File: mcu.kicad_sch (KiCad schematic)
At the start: 30 parts, among them J301 CONN_MCU_SERIAL, J302 CONN_EXT, SW301 SW_RST, SW302 SW_BOOT0, U301 STM32F765IITx, Y301 25MHz

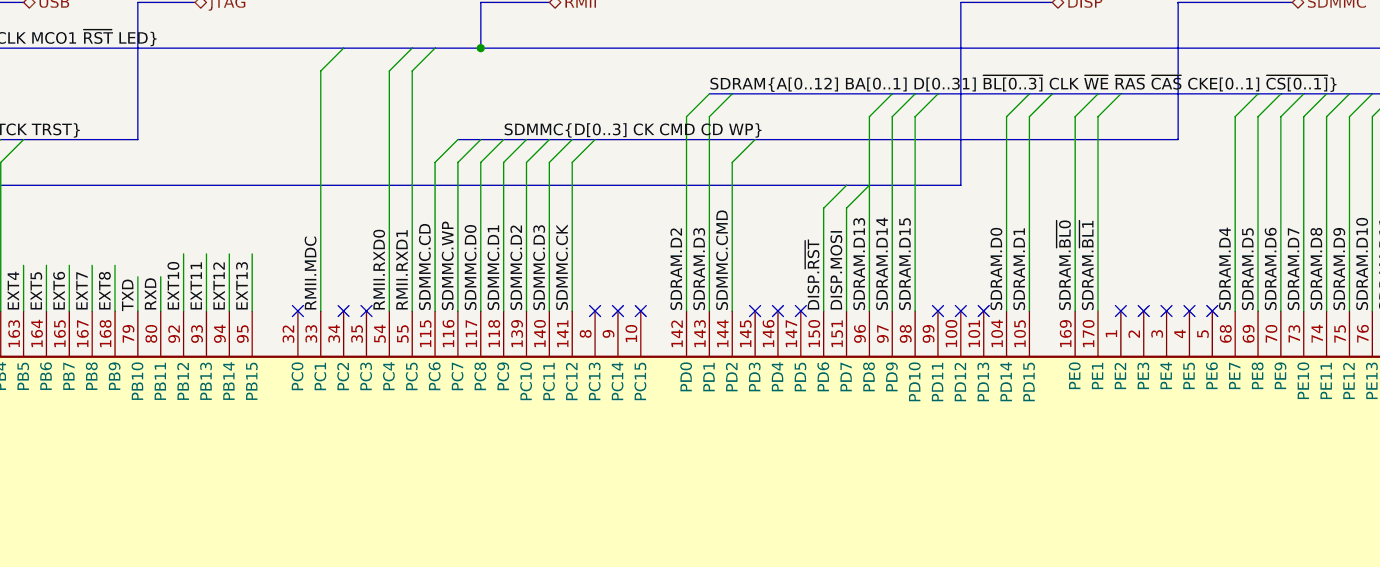
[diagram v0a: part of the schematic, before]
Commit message: Fix missing EXT9 connection, move EXT9-13 to PEx, route EXT connector.
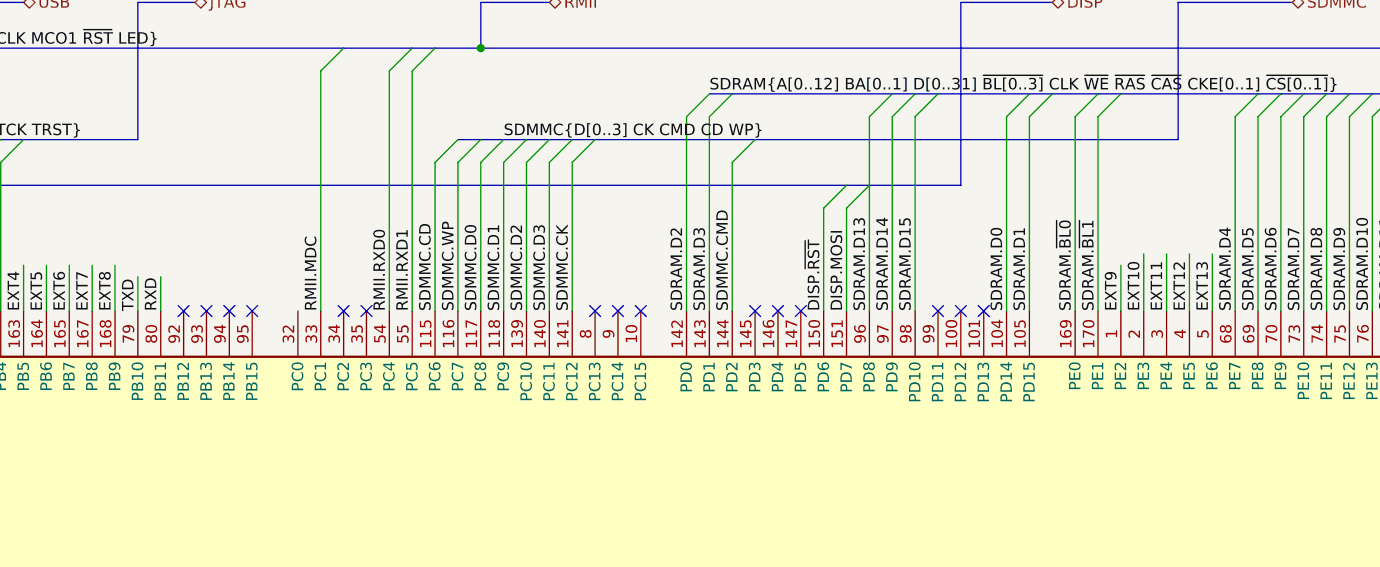
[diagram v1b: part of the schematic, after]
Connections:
- net EXT10: now also U301.2 (PE3); no longer U301.92 (PB12)
- net EXT11: now also U301.3 (PE4); no longer U301.93 (PB13)
- net EXT12: now also U301.4 (PE5); no longer U301.94 (PB14)
- net EXT13: now also U301.5 (PE6); no longer U301.95 (PB15)
- net EXT9: now also U301.1 (PE2)
- no-connect marks 26 -> 24
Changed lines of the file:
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@@
   (no_connect (at 176.53 50.8))
   (no_connect (at 207.01 124.46))
+  (no_connect (at 133.35 50.8))
   (no_connect (at 212.09 50.8))
   (no_connect (at 143.51 50.8))
@@
   (no_connect (at 250.19 124.46))
   (no_connect (at 212.09 124.46))
-  (no_connect (at 232.41 50.8))
   (no_connect (at 171.45 50.8))
-  (no_connect (at 237.49 50.8))
-  (no_connect (at 240.03 50.8))
   (no_connect (at 196.85 124.46))
-  (no_connect (at 229.87 50.8))
+  (no_connect (at 128.27 50.8))
   (no_connect (at 120.65 170.18))
-  (no_connect (at 234.95 50.8))
+  (no_connect (at 125.73 50.8))
   (no_connect (at 194.31 50.8))
   (no_connect (at 189.23 124.46))
@@
   (no_connect (at 191.77 50.8))
   (no_connect (at 204.47 124.46))
-  (no_connect (at 138.43 50.8))
+  (no_connect (at 130.81 50.8))
   (bus_entry (at 82.55 26.67) (size -2.54 2.54)
     (stroke (width 0) (type default) (color 0 0 0 0))
@@
     (stroke (width 0) (type default) (color 0 0 0 0))
   )
+  (wire (pts (xy 234.95 44.45) (xy 234.95 50.8))
+    (stroke (width 0) (type default) (color 0 0 0 0))
+  )
   (wire (pts (xy 123.19 46.99) (xy 123.19 50.8))
     (stroke (width 0) (type default) (color 0 0 0 0))
@@
     (stroke (width 0) (type default) (color 0 0 0 0))
   )
+  (wire (pts (xy 232.41 44.45) (xy 232.41 50.8))
+    (stroke (width 0) (type default) (color 0 0 0 0))
+  )
   (wire (pts (xy 130.81 124.46) (xy 130.81 139.7))
     (stroke (width 0) (type default) (color 0 0 0 0))
@@
     (stroke (width 0) (type default) (color 0 0 0 0))
   )
+  (wire (pts (xy 229.87 45.72) (xy 229.87 50.8))
+    (stroke (width 0) (type default) (color 0 0 0 0))
+  )
   (bus (pts (xy 269.24 16.51) (xy 273.05 16.51))
     (stroke (width 0) (type default) (color 0 0 0 0))
@@
     (stroke (width 0) (type default) (color 0 0 0 0))
   )
+  (wire (pts (xy 240.03 44.45) (xy 240.03 50.8))
+    (stroke (width 0) (type default) (color 0 0 0 0))
+  )
   (wire (pts (xy 217.17 29.21) (xy 217.17 50.8))
     (stroke (width 0) (type default) (color 0 0 0 0))
@@
     (stroke (width 0) (type default) (color 0 0 0 0))
   )
-  (wire (pts (xy 125.73 44.45) (xy 125.73 50.8))
-    (stroke (width 0) (type default) (color 0 0 0 0))
-  )
   (wire (pts (xy 166.37 124.46) (xy 166.37 137.16))
     (stroke (width 0) (type default) (color 0 0 0 0))
@@
     (stroke (width 0) (type default) (color 0 0 0 0))
   )
-  (wire (pts (xy 130.81 44.45) (xy 130.81 50.8))
-    (stroke (width 0) (type default) (color 0 0 0 0))
-  )
   (bus (pts (xy 151.13 21.59) (xy 153.67 21.59))
     (stroke (width 0) (type default) (color 0 0 0 0))
@@
     (stroke (width 0) (type default) (color 0 0 0 0))
   )
-  (wire (pts (xy 128.27 44.45) (xy 128.27 50.8))
-    (stroke (width 0) (type default) (color 0 0 0 0))
-  )
   (wire (pts (xy 196.85 39.37) (xy 196.85 50.8))
     (stroke (width 0) (type default) (color 0 0 0 0))
@@
     (stroke (width 0) (type default) (color 0 0 0 0))
   )
+  (wire (pts (xy 237.49 44.45) (xy 237.49 50.8))
+    (stroke (width 0) (type default) (color 0 0 0 0))
+  )
   (bus (pts (xy 120.65 16.51) (xy 120.65 31.75))
     (stroke (width 0) (type default) (color 0 0 0 0))
@@
     (stroke (width 0) (type default) (color 0 0 0 0))
   )
-  (wire (pts (xy 133.35 44.45) (xy 133.35 50.8))
-    (stroke (width 0) (type default) (color 0 0 0 0))
-  )
   (wire (pts (xy 33.02 48.26) (xy 41.91 48.26))
     (stroke (width 0) (type default) (color 0 0 0 0))
@@
     (effects (font (size 1.27 1.27)) (justify left bottom))
   )
-  (label "EXT12" (at 130.81 50.8 90)
-    (effects (font (size 1.27 1.27)) (justify left bottom))
-  )
   (label "SDRAM.A4" (at 234.95 124.46 270)
     (effects (font (size 1.27 1.27)) (justify right bottom))
@@
     (effects (font (size 1.27 1.27)) (justify left bottom))
   )
+  (label "EXT11" (at 234.95 50.8 90)
+    (effects (font (size 1.27 1.27)) (justify left bottom))
+  )
   (label "RMII.RXD0" (at 148.59 50.8 90)
     (effects (font (size 1.27 1.27)) (justify left bottom))
@@
     (effects (font (size 1.27 1.27)) (justify left bottom))
   )
+  (label "EXT12" (at 237.49 50.8 90)
+    (effects (font (size 1.27 1.27)) (justify left bottom))
+  )
+  (label "EXT9" (at 229.87 50.8 90)
+    (effects (font (size 1.27 1.27)) (justify left bottom))
+  )
   (label "SDRAM.D14" (at 204.47 50.8 90)
     (effects (font (size 1.27 1.27)) (justify left bottom))
@@
   (label "EXT8" (at 151.13 173.99 180)
     (effects (font (size 1.27 1.27)) (justify right bottom))
-  )
-  (label "EXT11" (at 128.27 50.8 90)
-    (effects (font (size 1.27 1.27)) (justify left bottom))
   )
   (label "EXT4" (at 151.13 163.83 180)
@@
     (effects (font (size 1.27 1.27)) (justify right bottom))
   )
-  (label "EXT13" (at 133.35 50.8 90)
-    (effects (font (size 1.27 1.27)) (justify left bottom))
-  )
   (label "SDRAM.D25" (at 107.95 124.46 270)
     (effects (font (size 1.27 1.27)) (justify right bottom))
@@
     (effects (font (size 1.27 1.27)) (justify left bottom))
   )
+  (label "EXT10" (at 232.41 50.8 90)
+    (effects (font (size 1.27 1.27)) (justify left bottom))
+  )
   (label "SDRAM.BA0" (at 191.77 124.46 270)
     (effects (font (size 1.27 1.27)) (justify right bottom))
@@
     (effects (font (size 1.27 1.27)) (justify left bottom))
   )
-  (label "EXT10" (at 125.73 50.8 90)
-    (effects (font (size 1.27 1.27)) (justify left bottom))
-  )
   (label "EXT3" (at 151.13 161.29 180)
     (effects (font (size 1.27 1.27)) (justify right bottom))
@@
     (effects (font (size 1.27 1.27)) (justify left bottom))
   )
+  (label "EXT13" (at 240.03 50.8 90)
+    (effects (font (size 1.27 1.27)) (justify left bottom))
+  )

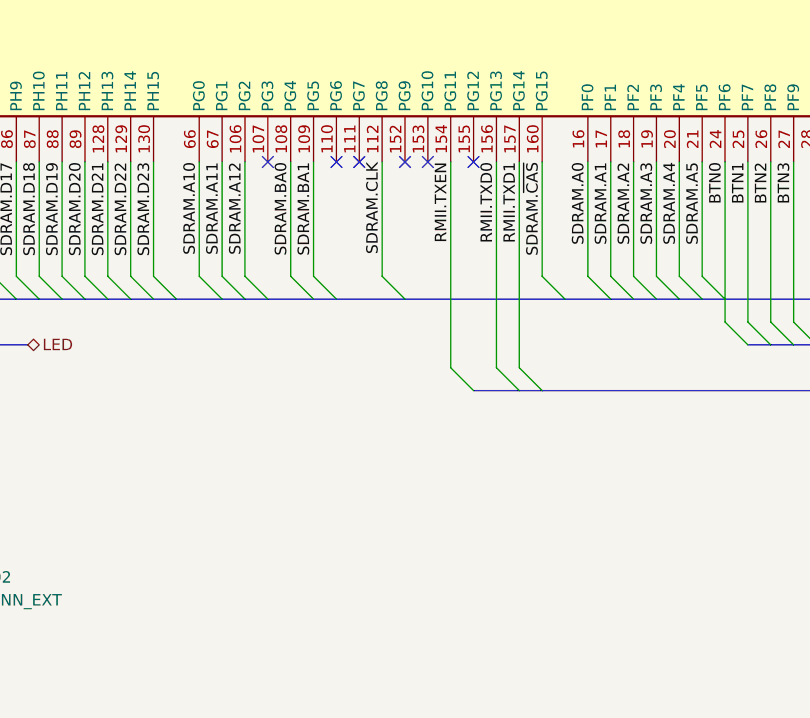
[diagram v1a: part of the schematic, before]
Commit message: Delay line for SDRAM CLK.
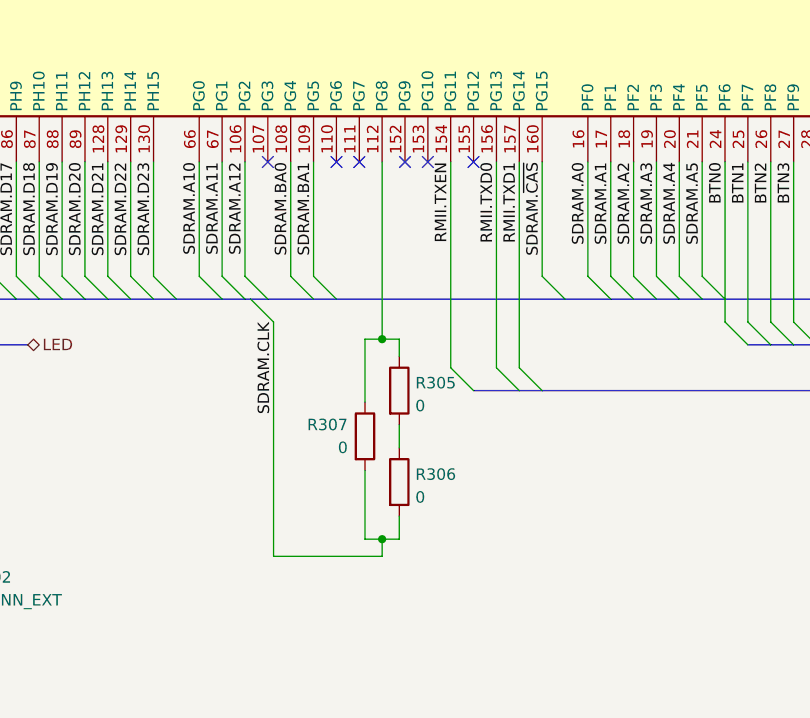
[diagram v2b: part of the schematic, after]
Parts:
- added R305, R306, R307: 0, Resistor_SMD:R_0603_1608Metric_Pad0.98x0.95mm_HandSolder, symbol Device:R
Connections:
- net SDRAM.CLK: now also R306.2, R307.2; no longer U301.112 (PG8)
- new net: R305.2, R306.1
- new net: R305.1, R307.1, U301.112 (PG8)
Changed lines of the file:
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@@
   (junction (at 274.32 83.82) (diameter 0) (color 0 0 0 0)
   )
+  (junction (at 201.93 144.145) (diameter 0) (color 0 0 0 0)
+  )
   (junction (at 97.79 173.99) (diameter 0) (color 0 0 0 0)
   )
@@
   )
   (junction (at 22.86 53.34) (diameter 0) (color 0 0 0 0)
+  )
+  (junction (at 201.93 166.37) (diameter 0) (color 0 0 0 0)
   )
   (junction (at 22.86 68.58) (diameter 0) (color 0 0 0 0)
@@
     (stroke (width 0) (type default) (color 0 0 0 0))
   )
-  (bus_entry (at 201.93 137.16) (size 2.54 2.54)
+  (bus_entry (at 187.325 139.7) (size 2.54 2.54)
     (stroke (width 0) (type default) (color 0 0 0 0))
   )
@@
     (stroke (width 0) (type default) (color 0 0 0 0))
   )
+  (wire (pts (xy 201.93 166.37) (xy 203.835 166.37))
+    (stroke (width 0) (type default) (color 0 0 0 0))
+  )
   (bus (pts (xy 156.21 31.75) (xy 158.75 31.75))
     (stroke (width 0) (type default) (color 0 0 0 0))
@@
     (stroke (width 0) (type default) (color 0 0 0 0))
   )
+  (wire (pts (xy 203.835 163.83) (xy 203.835 166.37))
+    (stroke (width 0) (type default) (color 0 0 0 0))
+  )
   (wire (pts (xy 43.18 144.78) (xy 62.23 144.78))
     (stroke (width 0) (type default) (color 0 0 0 0))
   )
+  (wire (pts (xy 203.835 153.67) (xy 203.835 156.21))
+    (stroke (width 0) (type default) (color 0 0 0 0))
+  )
   (wire (pts (xy 234.95 44.45) (xy 234.95 50.8))
     (stroke (width 0) (type default) (color 0 0 0 0))
@@
     (stroke (width 0) (type default) (color 0 0 0 0))
   )
-  (wire (pts (xy 201.93 124.46) (xy 201.93 137.16))
+  (wire (pts (xy 201.93 166.37) (xy 201.93 168.275))
     (stroke (width 0) (type default) (color 0 0 0 0))
   )
@@
     (stroke (width 0) (type default) (color 0 0 0 0))
   )
+  (wire (pts (xy 189.865 168.275) (xy 201.93 168.275))
+    (stroke (width 0) (type default) (color 0 0 0 0))
+  )
   (bus (pts (xy 77.47 26.67) (xy 80.01 26.67))
     (stroke (width 0) (type default) (color 0 0 0 0))
@@
     (stroke (width 0) (type default) (color 0 0 0 0))
   )
+  (wire (pts (xy 200.025 158.75) (xy 200.025 166.37))
+    (stroke (width 0) (type default) (color 0 0 0 0))
+  )
   (wire (pts (xy 130.81 124.46) (xy 130.81 139.7))
     (stroke (width 0) (type default) (color 0 0 0 0))
@@
     (stroke (width 0) (type default) (color 0 0 0 0))
   )
+  (wire (pts (xy 200.025 166.37) (xy 201.93 166.37))
+    (stroke (width 0) (type default) (color 0 0 0 0))
+  )
   (wire (pts (xy 22.86 53.34) (xy 22.86 48.26))
     (stroke (width 0) (type default) (color 0 0 0 0))
@@
     (stroke (width 0) (type default) (color 0 0 0 0))
   )
+  (bus (pts (xy 196.85 139.7) (xy 222.25 139.7))
+    (stroke (width 0) (type default) (color 0 0 0 0))
+  )
   (bus (pts (xy 163.83 139.7) (xy 166.37 139.7))
     (stroke (width 0) (type default) (color 0 0 0 0))
@@
     (stroke (width 0) (type default) (color 0 0 0 0))
   )
-  (bus (pts (xy 186.69 139.7) (xy 189.23 139.7))
+  (bus (pts (xy 186.69 139.7) (xy 187.325 139.7))
     (stroke (width 0) (type default) (color 0 0 0 0))
   )
@@
     (stroke (width 0) (type default) (color 0 0 0 0))
   )
+  (wire (pts (xy 200.025 144.145) (xy 200.025 151.13))
+    (stroke (width 0) (type default) (color 0 0 0 0))
+  )
   (wire (pts (xy 115.57 187.96) (xy 120.65 187.96))
     (stroke (width 0) (type default) (color 0 0 0 0))
@@
     (stroke (width 0) (type default) (color 0 0 0 0))
   )
+  (wire (pts (xy 201.93 144.145) (xy 203.835 144.145))
+    (stroke (width 0) (type default) (color 0 0 0 0))
+  )
   (wire (pts (xy 115.57 124.46) (xy 115.57 137.16))
     (stroke (width 0) (type default) (color 0 0 0 0))
@@
     (stroke (width 0) (type default) (color 0 0 0 0))
   )
-  (bus (pts (xy 196.85 139.7) (xy 204.47 139.7))
-    (stroke (width 0) (type default) (color 0 0 0 0))
-  )
   (wire (pts (xy 97.79 173.99) (xy 97.79 180.34))
     (stroke (width 0) (type default) (color 0 0 0 0))
@@
     (stroke (width 0) (type default) (color 0 0 0 0))
   )
+  (wire (pts (xy 189.865 168.275) (xy 189.865 142.24))
+    (stroke (width 0) (type default) (color 0 0 0 0))
+  )
   (wire (pts (xy 31.75 128.27) (xy 31.75 134.62))
     (stroke (width 0) (type default) (color 0 0 0 0))
@@
     (stroke (width 0) (type default) (color 0 0 0 0))
   )
+  (wire (pts (xy 201.93 124.46) (xy 201.93 144.145))
+    (stroke (width 0) (type default) (color 0 0 0 0))
+  )
   (wire (pts (xy 38.1 83.82) (xy 41.91 83.82))
     (stroke (width 0) (type default) (color 0 0 0 0))
@@
     (stroke (width 0) (type default) (color 0 0 0 0))
   )
+  (wire (pts (xy 203.835 144.145) (xy 203.835 146.05))
+    (stroke (width 0) (type default) (color 0 0 0 0))
+  )
   (wire (pts (xy 115.57 186.69) (xy 115.57 187.96))
     (stroke (width 0) (type default) (color 0 0 0 0))
@@
     (stroke (width 0) (type default) (color 0 0 0 0))
   )
+  (wire (pts (xy 200.025 144.145) (xy 201.93 144.145))
+    (stroke (width 0) (type default) (color 0 0 0 0))
+  )
   (wire (pts (xy 22.86 68.58) (xy 25.4 68.58))
     (stroke (width 0) (type default) (color 0 0 0 0))
   )
+  (bus (pts (xy 187.325 139.7) (xy 189.23 139.7))
+    (stroke (width 0) (type default) (color 0 0 0 0))
+  )
   (wire (pts (xy 125.73 153.67) (xy 125.73 162.56))
     (stroke (width 0) (type default) (color 0 0 0 0))
@@
     (stroke (width 0) (type default) (color 0 0 0 0))
   )
-  (bus (pts (xy 204.47 139.7) (xy 222.25 139.7))
-    (stroke (width 0) (type default) (color 0 0 0 0))
-  )
   (label "JTAG.TCK" (at 87.63 50.8 90)
     (effects (font (size 1.27 1.27)) (justify left bottom))
@@
     (effects (font (size 1.27 1.27)) (justify right bottom))
   )
-  (label "SDRAM.CLK" (at 201.93 124.46 270)
-    (effects (font (size 1.27 1.27)) (justify right bottom))
-  )
   (label "SDMMC.D3" (at 166.37 50.8 90)
     (effects (font (size 1.27 1.27)) (justify left bottom))
@@
   (label "USB{VBUS DM DP ID}" (at 77.47 26.67 0)
     (effects (font (size 1.27 1.27)) (justify left bottom))
+  )
+  (label "SDRAM.CLK" (at 189.865 142.24 270)
+    (effects (font (size 1.27 1.27)) (justify right bottom))
   )
   (label "RMII{TXEN TXD[0..1] RXD[0..1] CRSDV MDC MDIO REFCLK MCO1 ~{RST} LED}"
@@
     )
     (pin "1")
+  )
+  (symbol (lib_id "Device:R") (at 203.835 160.02 0) (unit 1)
+    (in_bom yes) (on_board yes) (fields_autoplaced)
+    (property "Reference" "R306" (id 0) (at 205.613 159.1853 0)
+      (effects (font (size 1.27 1.27)) (justify left))
+    )
+    (property "Value" "0" (id 1) (at 205.613 161.7222 0)
+      (effects (font (size 1.27 1.27)) (justify left))
+    )
+    (property "Footprint" "Resistor_SMD:R_0603_1608Metric_Pad0.98x0.95mm_HandSolder" (id 2) (at 202.057 160.02 90)
+      (effects (font (size 1.27 1.27)) hide)
+    )
+    (property "Datasheet" "~" (id 3) (at 203.835 160.02 0)
+      (effects (font (size 1.27 1.27)) hide)
+    )
+    (pin "1")
+    (pin "2")
   )
   (symbol (lib_id "Device:R") (at 39.37 134.62 90) (unit 1)
@@
     (pin "2")
   )
+  (symbol (lib_id "Device:R") (at 200.025 154.94 0) (unit 1)
+    (in_bom yes) (on_board yes)
+    (property "Reference" "R307" (id 0) (at 198.12 153.67 0)
+      (effects (font (size 1.27 1.27)) (justify right))
+    )
+    (property "Value" "0" (id 1) (at 198.12 156.21 0)
+      (effects (font (size 1.27 1.27)) (justify right))
+    )
+    (property "Footprint" "Resistor_SMD:R_0603_1608Metric_Pad0.98x0.95mm_HandSolder" (id 2) (at 198.247 154.94 90)
+      (effects (font (size 1.27 1.27)) hide)
+    )
+    (property "Datasheet" "~" (id 3) (at 200.025 154.94 0)
+      (effects (font (size 1.27 1.27)) hide)
+    )
+    (pin "1")
+    (pin "2")
+  )
   (symbol (lib_id "power:GND") (at 67.31 142.24 0) (unit 1)
     (in_bom yes) (on_board yes) (fields_autoplaced)
@@
     (pin "1")
   )
+  (symbol (lib_id "Device:R") (at 203.835 149.86 0) (unit 1)
+    (in_bom yes) (on_board yes) (fields_autoplaced)
+    (property "Reference" "R305" (id 0) (at 205.613 149.0253 0)
+      (effects (font (size 1.27 1.27)) (justify left))
+    )
+    (property "Value" "0" (id 1) (at 205.613 151.5622 0)
+      (effects (font (size 1.27 1.27)) (justify left))
+    )
+    (property "Footprint" "Resistor_SMD:R_0603_1608Metric_Pad0.98x0.95mm_HandSolder" (id 2) (at 202.057 149.86 90)
+      (effects (font (size 1.27 1.27)) hide)
+    )
+    (property "Datasheet" "~" (id 3) (at 203.835 149.86 0)
+      (effects (font (size 1.27 1.27)) hide)
+    )
+    (pin "1")
+    (pin "2")
+  )
 )
